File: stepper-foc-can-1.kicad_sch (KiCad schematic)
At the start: 57 parts, among them J1 TC2030, J2 Conn_01x02, J4 Conn_01x04_Pin, J5 Conn_01x02, J6 Conn_01x02, SW1 SW_Push, SW2 SW_Push, SW3 SW_Push, U1 STM32G474RBTx, U2 MX25947, U3 TPS62933, U4 AS5047P, U9 TCAN3413, Y1 Crystal_GND24

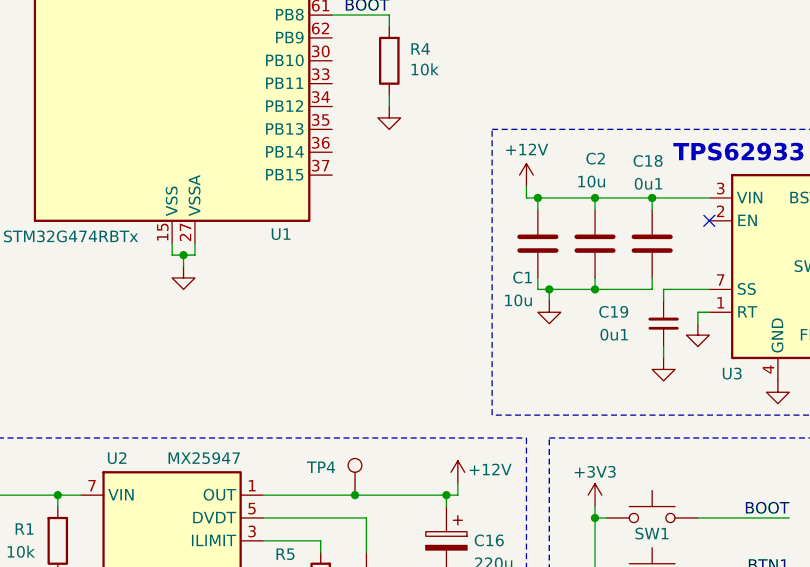
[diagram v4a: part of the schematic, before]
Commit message: schem: add can led
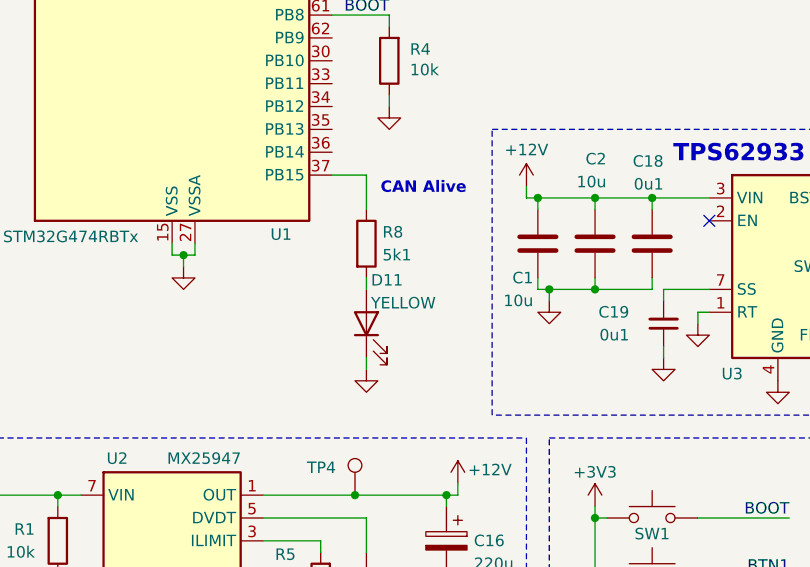
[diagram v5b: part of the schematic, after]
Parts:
- added D11: YELLOW, LED_SMD:LED_0805_2012Metric, symbol Device:LED
- added R8: 5k1, Resistor_SMD:R_0402_1005Metric, symbol Device:R
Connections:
- net GND: now also D11.1 (K)
- net at U1.37 (PB15): now also R8.1
- new net: D11.2 (A), R8.2
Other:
- note added: "CAN Alive"

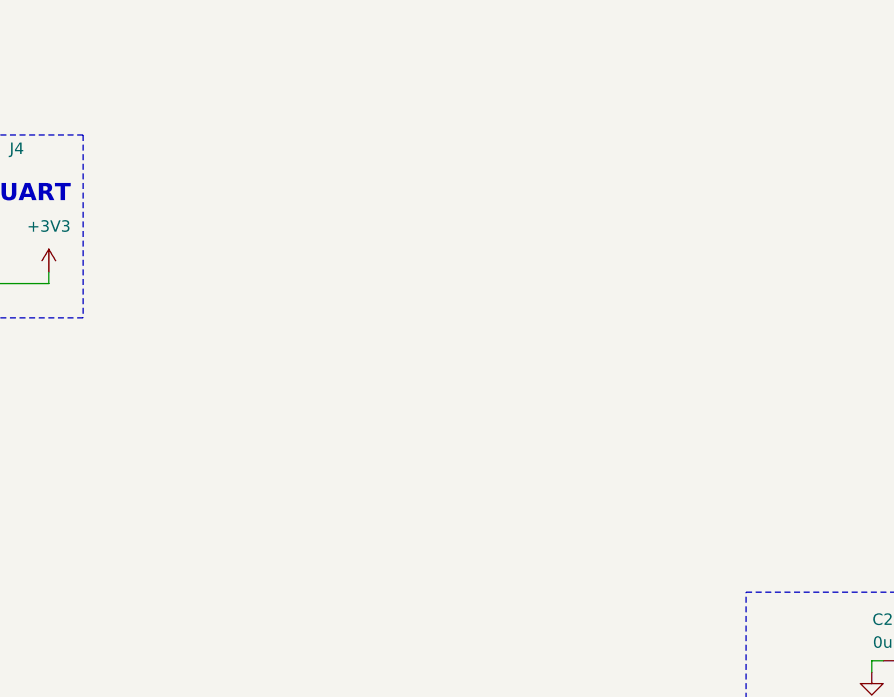
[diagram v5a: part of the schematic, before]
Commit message: schem: add DRV8874 h bridge driver
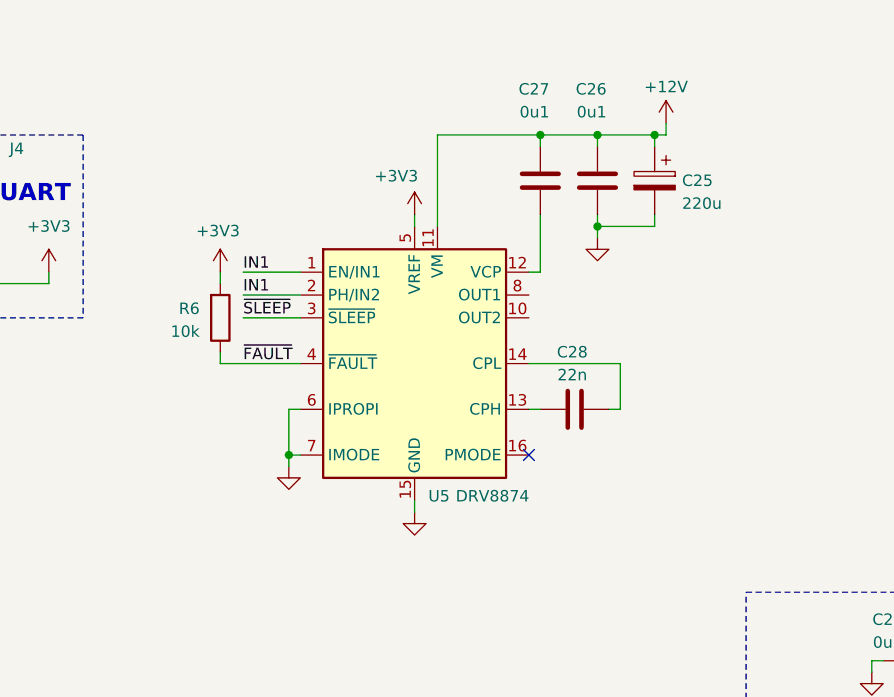
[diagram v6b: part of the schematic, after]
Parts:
- added C25: 220u, Capacitor_SMD:CP_Elec_6.3x7.7, symbol Device:C_Polarized
- added C26, C27: 0u1, Capacitor_SMD:C_0402_1005Metric, symbol Device:C
- added C28: 22n, Capacitor_SMD:C_0603_1608Metric, symbol Device:C
- added R6: 10k, Resistor_SMD:R_0402_1005Metric, symbol Device:R
- added U5: DRV8874, Package_SO:HTSSOP-16-1EP_4.4x5mm_P0.65mm_EP3.4x5mm_Mask2.46x2.31mm_ThermalVias, symbol GLCS:DRV8874
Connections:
- net +12V: now also C25.1, C26.1, C27.1, U5.11 (VM)
- net +3V3: now also R6.2, U5.5 (VREF)
- net GND: now also C25.2, C26.2, U5.15 (GND), U5.6 (IPROPI), U5.7 (IMODE), U5.9 (PGND)
- new net: C27.2, U5.12 (VCP)
- new net: C28.1, U5.13 (CPH)
- new net: C28.2, U5.14 (CPL)
- new net IN1: U5.1 (EN/IN1), U5.2 (PH/IN2)
- new net ~{FAULT}: R6.1, U5.4 (~{FAULT})
- new net ~{SLEEP}: U5.3 (~{SLEEP})
- no-connect marks 5 -> 6

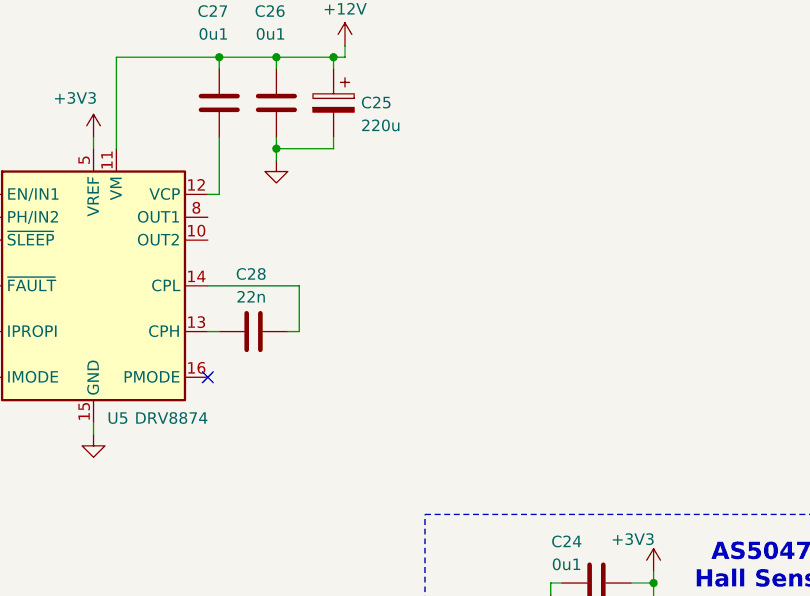
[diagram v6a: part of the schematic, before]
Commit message: schem: add INA241A ultra precision current sense amp
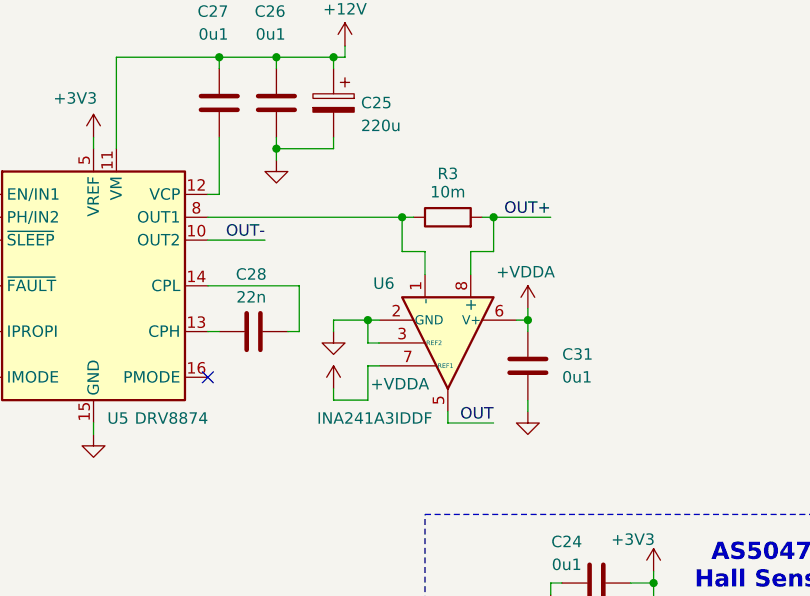
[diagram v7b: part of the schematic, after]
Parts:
- added C31: 0u1, Capacitor_SMD:C_0402_1005Metric, symbol Device:C
- added R3: 10m, symbol Device:R
- added U6: INA241A3IDDF, Package_TO_SOT_SMD:SOT-23-8, symbol Amplifier_Current:INA241A3xDDF
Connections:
- net +VDDA: now also C31.1, U6.6 (V+), U6.7 (REF1)
- net GND: now also C31.2, U6.2 (GND), U6.3 (REF2), U6.4 (GND)
- net OUT-: now reaches U5.10 (OUT2)
- net at U5.8 (OUT1): now also R3.1, U6.1 (-)
- new net OUT: U6.5
- new net OUT+: R3.2, U6.8 (+)

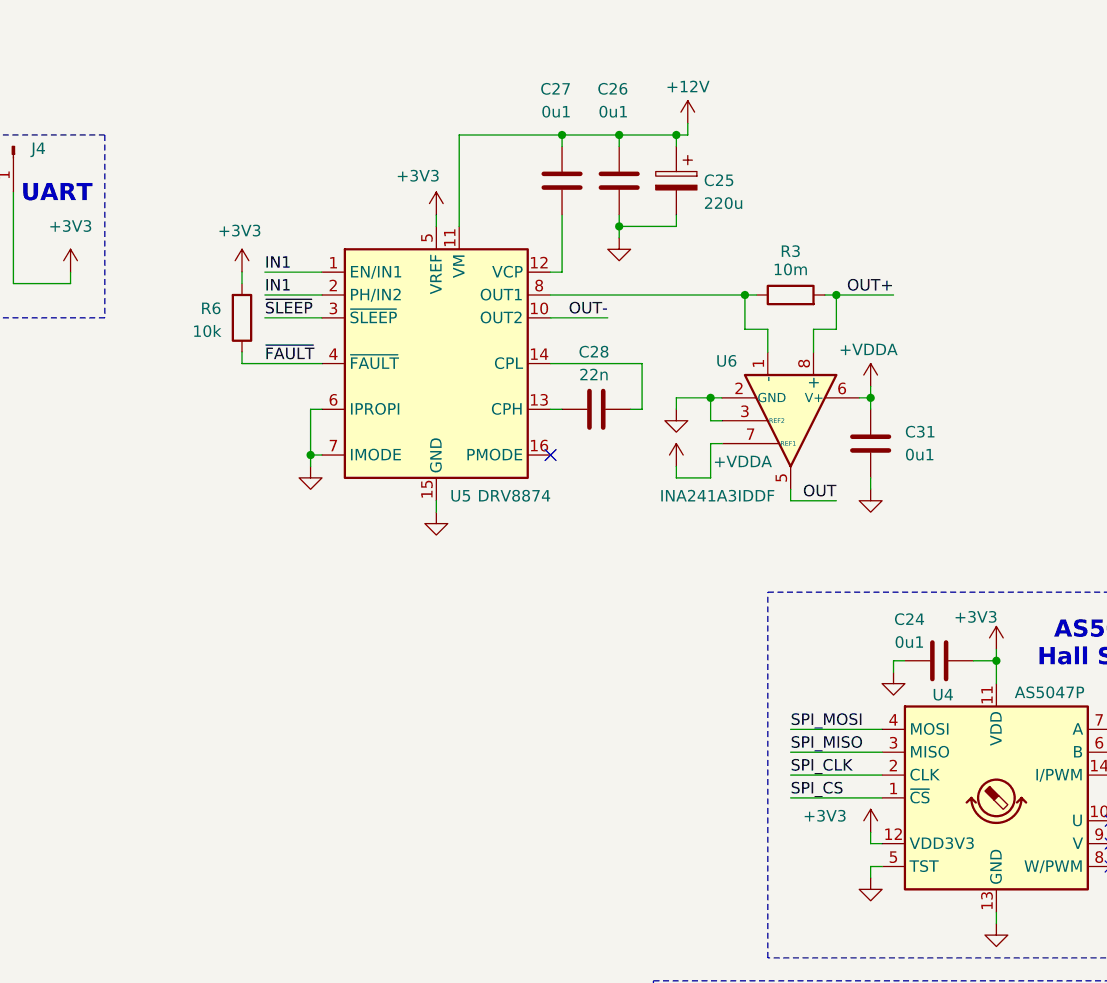
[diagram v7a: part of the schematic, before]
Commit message: schem: add second h bridge and motor connector
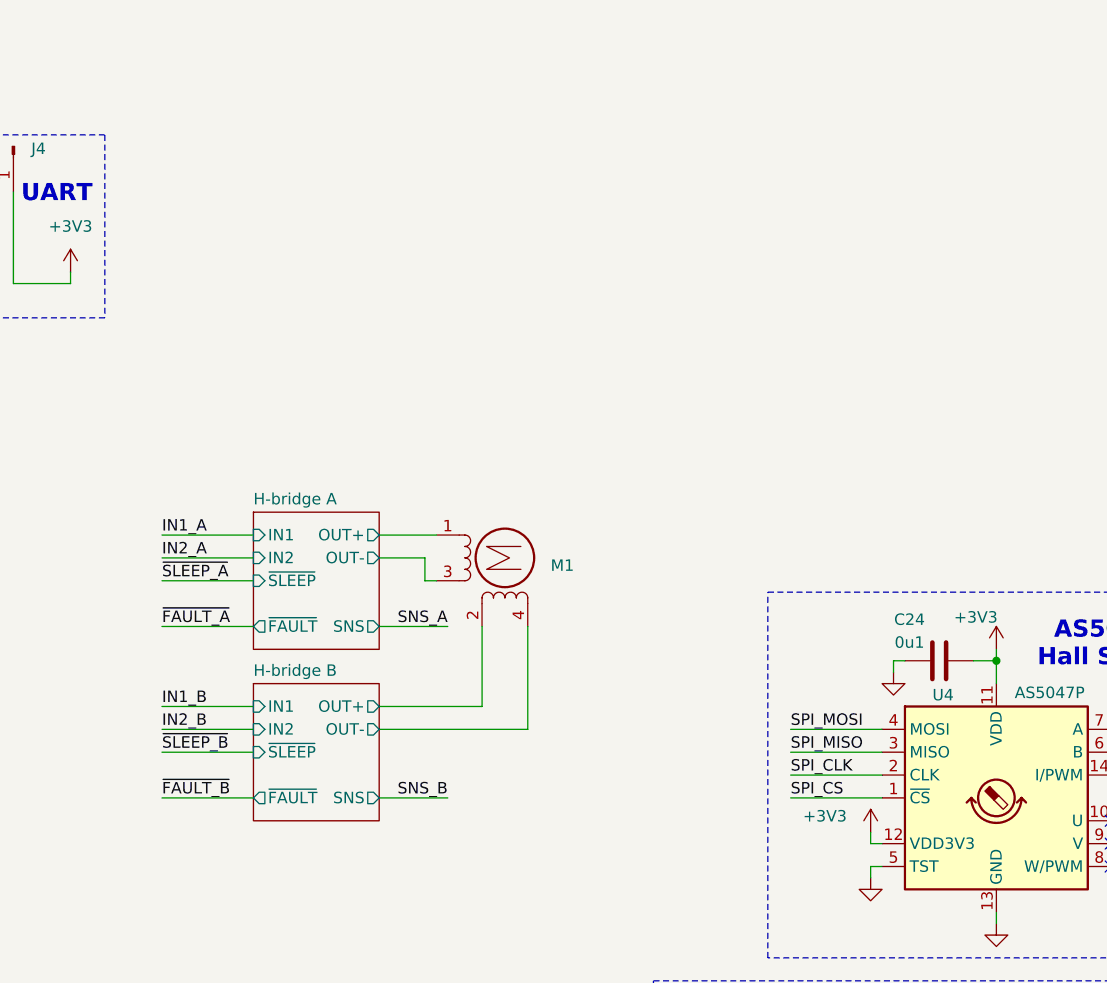
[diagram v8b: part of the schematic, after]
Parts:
- removed C25: 220u, Capacitor_SMD:CP_Elec_6.3x7.7, symbol Device:C_Polarized
- removed C26, C27, C31: 0u1, Capacitor_SMD:C_0402_1005Metric, symbol Device:C
- removed C28: 22n, Capacitor_SMD:C_0603_1608Metric, symbol Device:C
- removed R3: 10m, symbol Device:R
- removed R6: 10k, Resistor_SMD:R_0402_1005Metric, symbol Device:R
- removed U5: DRV8874, Package_SO:HTSSOP-16-1EP_4.4x5mm_P0.65mm_EP3.4x5mm_Mask2.46x2.31mm_ThermalVias, symbol GLCS:DRV8874
- removed U6: INA241A3IDDF, Package_TO_SOT_SMD:SOT-23-8, symbol Amplifier_Current:INA241A3xDDF
- added M1: Stepper_Motor_bipolar, symbol Motor:Stepper_Motor_bipolar
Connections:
- new net H-bridge A/OUT+: M1.1 (-)
- new net H-bridge A/OUT-: M1.3
- new net H-bridge B/OUT+: M1.2
- new net H-bridge B/OUT-: M1.4
- no-connect marks 6 -> 5
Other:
- added sheet H-bridge A (h-bridge.kicad_sch)
- added sheet H-bridge B (h-bridge.kicad_sch)
